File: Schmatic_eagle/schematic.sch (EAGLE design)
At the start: 7 parts, among them IC1 MEGA16-M, IC2 MC145026D, M1 WIRELESS-XY-FST

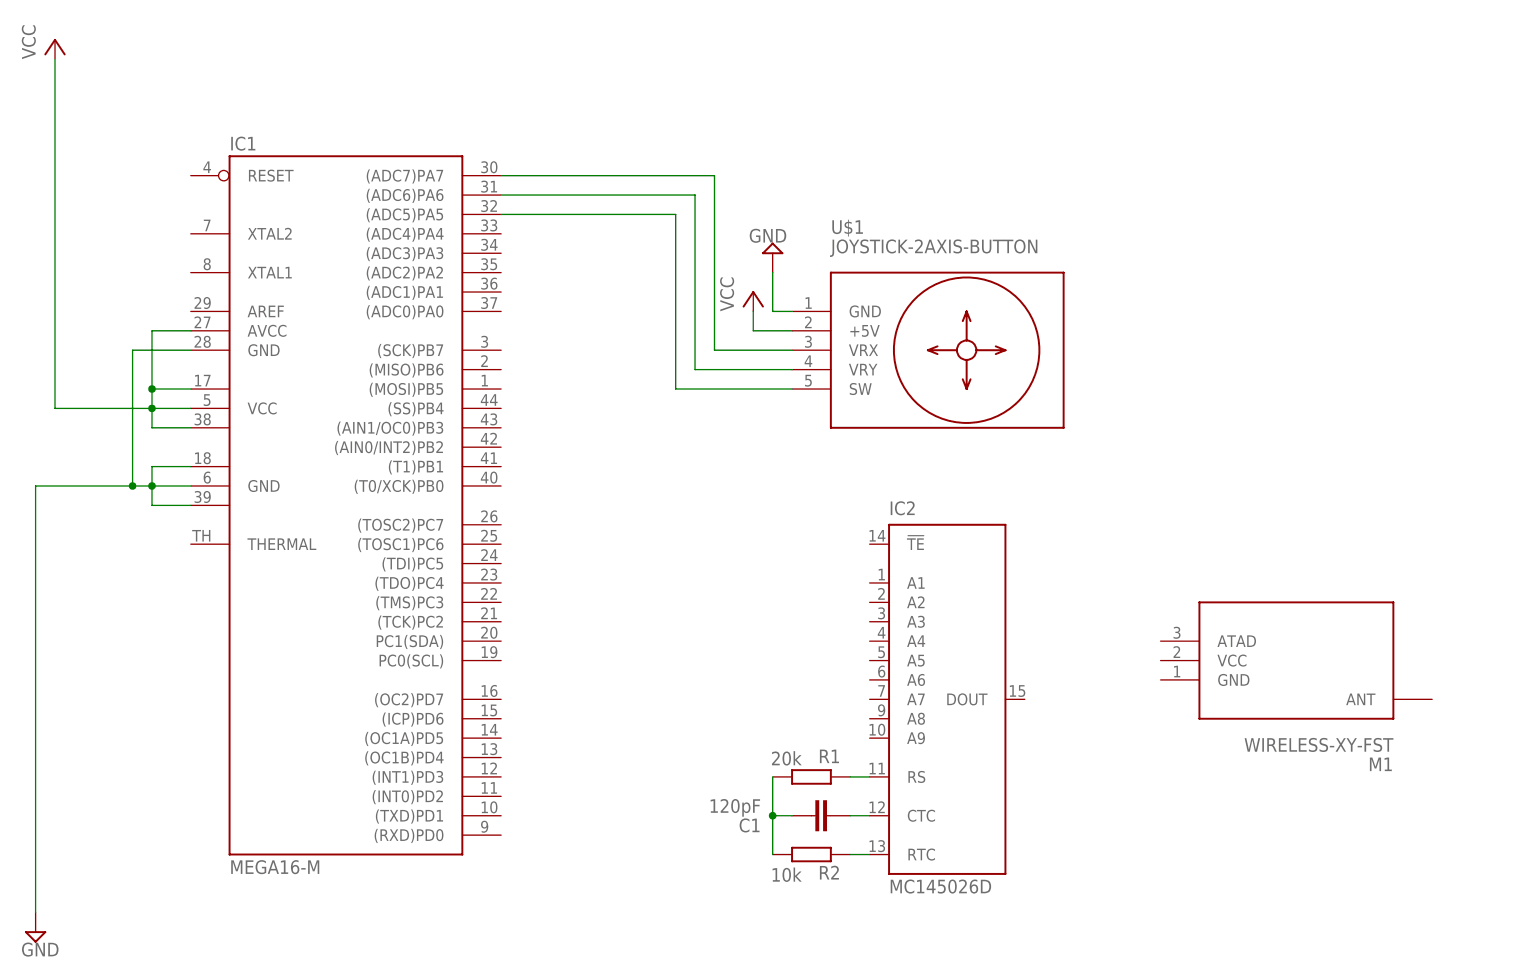
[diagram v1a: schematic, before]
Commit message: Schematic updates
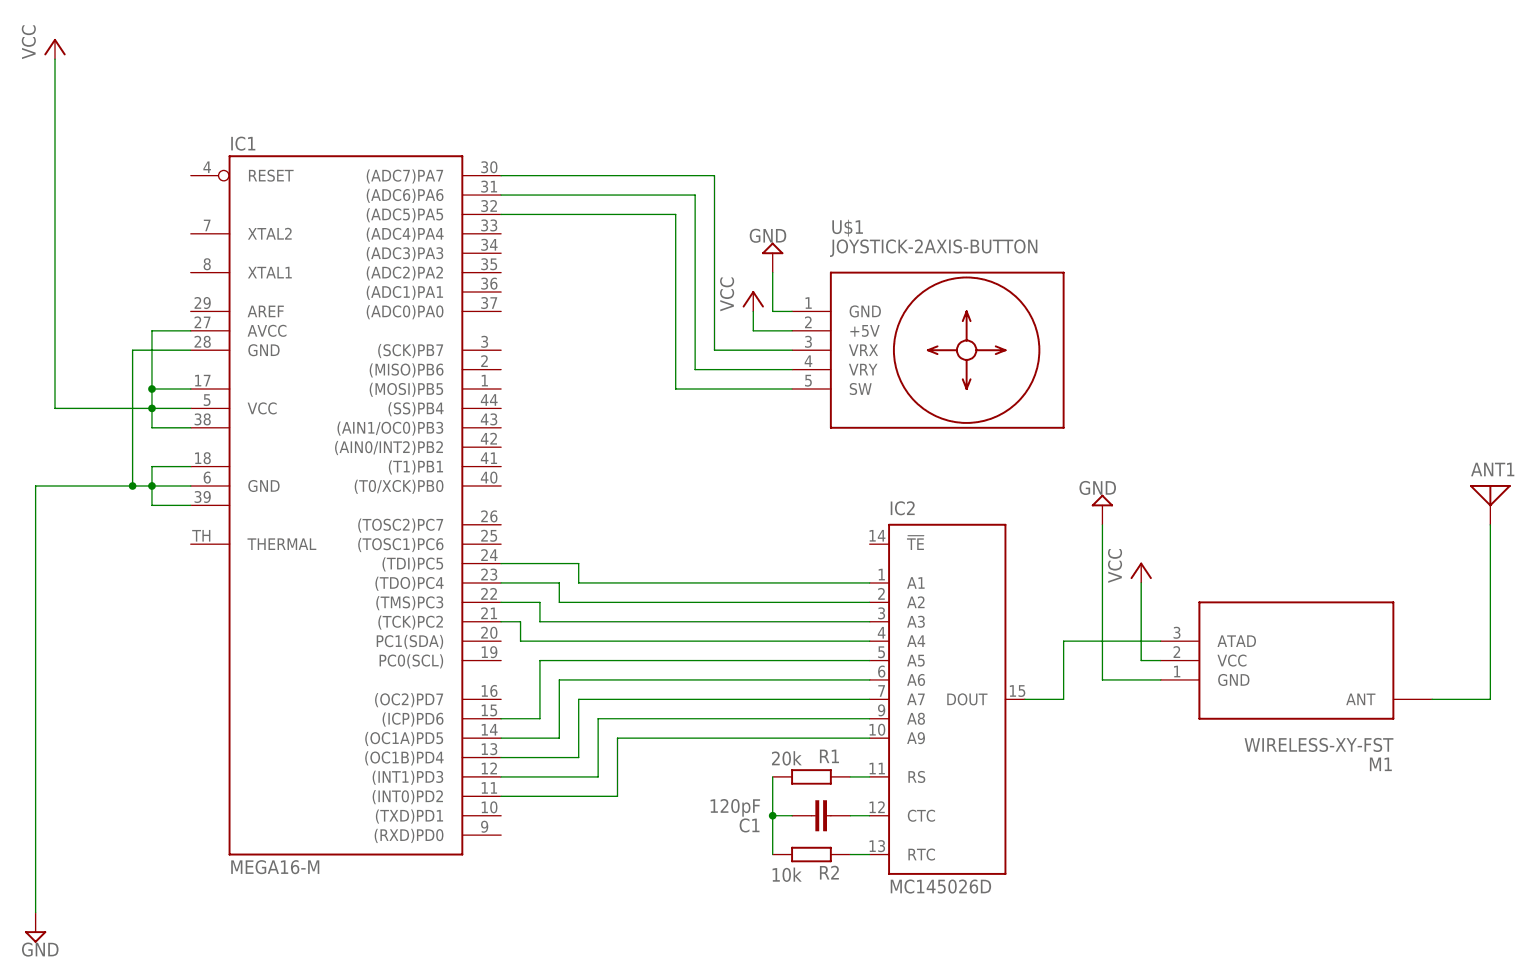
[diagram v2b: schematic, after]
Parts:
- added ANT1: (no value), discrete:ANTENNA
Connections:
- new net N$10: IC1.(OC1B)PD4, IC2G$1.A7
- new net N$11: IC1.(OC1A)PD5, IC2G$1.A6
- new net N$12: IC1.(ICP)PD6, IC2G$1.A5
- new net N$13: IC1.(INT0)PD2, IC2G$1.A9
- new net N$14: IC1.(INT1)PD3, IC2G$1.A8
- new net N$15: IC1.(TCK)PC2, IC2G$1.A4
- new net N$16: IC1.(TMS)PC3, IC2G$1.A3
- new net N$17: IC1.(TDO)PC4, IC2G$1.A2
- new net N$18: IC1.(TDI)PC5, IC2G$1.A1
- new net N$8: IC2G$1.DOUT, M1.ATAD
- new net N$9: ANT1.1, M1.ANT
- net GND: now also M1.GND
- net VCC: now also M1.VCC
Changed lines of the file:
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@@
 <part name="R1" library="rcl" library_urn="urn:adsk.eagle:library:334" deviceset="R-EU_" device="01005" package3d_urn="urn:adsk.eagle:package:26133/2" value="20k"/>
 <part name="R2" library="rcl" library_urn="urn:adsk.eagle:library:334" deviceset="R-EU_" device="01005" package3d_urn="urn:adsk.eagle:package:26133/2" value="10k"/>
+<part name="P+3" library="supply1" library_urn="urn:adsk.eagle:library:371" deviceset="VCC" device=""/>
+<part name="SUPPLY3" library="supply2" library_urn="urn:adsk.eagle:library:372" deviceset="GND" device=""/>
+<part name="ANT1" library="discrete" library_urn="urn:adsk.eagle:library:211" deviceset="ANTENNA" device="" package3d_urn="urn:adsk.eagle:package:12928/1"/>
 </parts>
 <sheets>
@@
 <attribute name="NAME" x="229.87" y="67.0814" size="1.778" layer="95" rot="R180"/>
 <attribute name="VALUE" x="224.79" y="66.802" size="1.778" layer="96" rot="R180"/>
+</instance>
+<instance part="P+3" gate="VCC" x="269.24" y="106.68" smashed="yes">
+<attribute name="VALUE" x="266.7" y="104.14" size="1.778" layer="96" rot="R90"/>
+</instance>
+<instance part="SUPPLY3" gate="GND" x="264.16" y="114.3" smashed="yes" rot="R180">
+<attribute name="VALUE" x="266.065" y="117.475" size="1.778" layer="96" rot="R180"/>
+</instance>
+<instance part="ANT1" gate="A" x="314.96" y="116.84" smashed="yes">
+<attribute name="NAME" x="312.42" y="118.11" size="1.778" layer="95"/>
+<attribute name="VALUE" x="317.5" y="111.76" size="1.778" layer="96"/>
 </instance>
 </instances>
@@
 <wire x1="139.7" y1="137.16" x2="139.7" y2="129.54" width="0.1524" layer="91"/>
 <junction x="139.7" y="129.54"/>
+</segment>
+<segment>
+<pinref part="P+3" gate="VCC" pin="VCC"/>
+<wire x1="269.24" y1="104.14" x2="269.24" y2="93.98" width="0.1524" layer="91"/>
+<pinref part="M1" gate="G$1" pin="VCC"/>
+<wire x1="269.24" y1="93.98" x2="271.78" y2="93.98" width="0.1524" layer="91"/>
 </segment>
 </net>
@@
 <junction x="137.16" y="116.84"/>
 </segment>
+<segment>
+<pinref part="SUPPLY3" gate="GND" pin="GND"/>
+<pinref part="M1" gate="G$1" pin="GND"/>
+<wire x1="264.16" y1="111.76" x2="264.16" y2="91.44" width="0.1524" layer="91"/>
+<wire x1="264.16" y1="91.44" x2="271.78" y2="91.44" width="0.1524" layer="91"/>
+</segment>
 </net>
 <net name="N$4" class="0">
@@
 </segment>
 </net>
+<net name="N$8" class="0">
+<segment>
+<pinref part="M1" gate="G$1" pin="ATAD"/>
+<wire x1="271.78" y1="96.52" x2="259.08" y2="96.52" width="0.1524" layer="91"/>
+<wire x1="259.08" y1="96.52" x2="259.08" y2="88.9" width="0.1524" layer="91"/>
+<pinref part="IC2" gate="G$1" pin="DOUT"/>
+<wire x1="259.08" y1="88.9" x2="254" y2="88.9" width="0.1524" layer="91"/>
+</segment>
+</net>
+<net name="N$9" class="0">
+<segment>
+<pinref part="ANT1" gate="A" pin="1"/>
+<pinref part="M1" gate="G$1" pin="ANT"/>
+<wire x1="314.96" y1="111.76" x2="314.96" y2="88.9" width="0.1524" layer="91"/>
+<wire x1="314.96" y1="88.9" x2="307.34" y2="88.9" width="0.1524" layer="91"/>
+</segment>
+</net>
+<net name="N$13" class="0">
+<segment>
+<pinref part="IC2" gate="G$1" pin="A9"/>
+<wire x1="233.68" y1="83.82" x2="200.66" y2="83.82" width="0.1524" layer="91"/>
+<wire x1="200.66" y1="83.82" x2="200.66" y2="76.2" width="0.1524" layer="91"/>
+<pinref part="IC1" gate="G$1" pin="(INT0)PD2"/>
+<wire x1="200.66" y1="76.2" x2="185.42" y2="76.2" width="0.1524" layer="91"/>
+</segment>
+</net>
+<net name="N$14" class="0">
+<segment>
+<pinref part="IC2" gate="G$1" pin="A8"/>
+<wire x1="233.68" y1="86.36" x2="198.12" y2="86.36" width="0.1524" layer="91"/>
+<wire x1="198.12" y1="86.36" x2="198.12" y2="78.74" width="0.1524" layer="91"/>
+<pinref part="IC1" gate="G$1" pin="(INT1)PD3"/>
+<wire x1="198.12" y1="78.74" x2="185.42" y2="78.74" width="0.1524" layer="91"/>
+</segment>
+</net>
+<net name="N$10" class="0">
+<segment>
+<pinref part="IC1" gate="G$1" pin="(OC1B)PD4"/>
+<wire x1="185.42" y1="81.28" x2="195.58" y2="81.28" width="0.1524" layer="91"/>
+<wire x1="195.58" y1="81.28" x2="195.58" y2="88.9" width="0.1524" layer="91"/>
+<pinref part="IC2" gate="G$1" pin="A7"/>
+<wire x1="233.68" y1="88.9" x2="195.58" y2="88.9" width="0.1524" layer="91"/>
+</segment>
+</net>
+<net name="N$11" class="0">
+<segment>
+<pinref part="IC2" gate="G$1" pin="A6"/>
+<wire x1="233.68" y1="91.44" x2="193.04" y2="91.44" width="0.1524" layer="91"/>
+<wire x1="193.04" y1="91.44" x2="193.04" y2="83.82" width="0.1524" layer="91"/>
+<pinref part="IC1" gate="G$1" pin="(OC1A)PD5"/>
+<wire x1="193.04" y1="83.82" x2="185.42" y2="83.82" width="0.1524" layer="91"/>
+</segment>
+</net>
+<net name="N$12" class="0">
+<segment>
+<pinref part="IC2" gate="G$1" pin="A5"/>
+<wire x1="233.68" y1="93.98" x2="190.5" y2="93.98" width="0.1524" layer="91"/>
+<wire x1="190.5" y1="93.98" x2="190.5" y2="86.36" width="0.1524" layer="91"/>
+<pinref part="IC1" gate="G$1" pin="(ICP)PD6"/>
+<wire x1="190.5" y1="86.36" x2="185.42" y2="86.36" width="0.1524" layer="91"/>
+</segment>
+</net>
+<net name="N$15" class="0">
+<segment>
+<pinref part="IC2" gate="G$1" pin="A4"/>
+<wire x1="233.68" y1="96.52" x2="187.96" y2="96.52" width="0.1524" layer="91"/>
+<wire x1="187.96" y1="96.52" x2="187.96" y2="99.06" width="0.1524" layer="91"/>
+<pinref part="IC1" gate="G$1" pin="(TCK)PC2"/>
+<wire x1="187.96" y1="99.06" x2="185.42" y2="99.06" width="0.1524" layer="91"/>
+</segment>
+</net>
+<net name="N$16" class="0">
+<segment>
+<pinref part="IC1" gate="G$1" pin="(TMS)PC3"/>
+<wire x1="185.42" y1="101.6" x2="190.5" y2="101.6" width="0.1524" layer="91"/>
+<wire x1="190.5" y1="101.6" x2="190.5" y2="99.06" width="0.1524" layer="91"/>
+<pinref part="IC2" gate="G$1" pin="A3"/>
+<wire x1="190.5" y1="99.06" x2="233.68" y2="99.06" width="0.1524" layer="91"/>
+</segment>
+</net>
+<net name="N$17" class="0">
+<segment>
+<pinref part="IC1" gate="G$1" pin="(TDO)PC4"/>
+<wire x1="185.42" y1="104.14" x2="193.04" y2="104.14" width="0.1524" layer="91"/>
+<wire x1="193.04" y1="104.14" x2="193.04" y2="101.6" width="0.1524" layer="91"/>
+<pinref part="IC2" gate="G$1" pin="A2"/>
+<wire x1="193.04" y1="101.6" x2="233.68" y2="101.6" width="0.1524" layer="91"/>
+</segment>
+</net>
+<net name="N$18" class="0">
+<segment>
+<pinref part="IC1" gate="G$1" pin="(TDI)PC5"/>
+<wire x1="185.42" y1="106.68" x2="195.58" y2="106.68" width="0.1524" layer="91"/>
+<pinref part="IC2" gate="G$1" pin="A1"/>
+<wire x1="195.58" y1="106.68" x2="195.58" y2="104.14" width="0.1524" layer="91"/>
+<wire x1="195.58" y1="104.14" x2="233.68" y2="104.14" width="0.1524" layer="91"/>
+</segment>
+</net>

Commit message: Schematic updates
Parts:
- added C2: 0.1uF, capacitor-wima:C2,5-3
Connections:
- new net N$19: IC1.(TOSC1)PC6, IC2G$1.!TE
- net GND: now also C2.1
- net VCC: now also C2.2
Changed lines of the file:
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@@
 <part name="SUPPLY3" library="supply2" library_urn="urn:adsk.eagle:library:372" deviceset="GND" device=""/>
 <part name="ANT1" library="discrete" library_urn="urn:adsk.eagle:library:211" deviceset="ANTENNA" device="" package3d_urn="urn:adsk.eagle:package:12928/1"/>
+<part name="SUPPLY4" library="supply2" library_urn="urn:adsk.eagle:library:372" deviceset="GND" device=""/>
+<part name="P+4" library="supply1" library_urn="urn:adsk.eagle:library:371" deviceset="VCC" device=""/>
+<part name="C2" library="capacitor-wima" library_urn="urn:adsk.eagle:library:116" deviceset="C" device="2,5-3" package3d_urn="urn:adsk.eagle:package:5436/1" value="0.1uF"/>
 </parts>
 <sheets>
@@
 <attribute name="NAME" x="312.42" y="118.11" size="1.778" layer="95"/>
 <attribute name="VALUE" x="317.5" y="111.76" size="1.778" layer="96"/>
+</instance>
+<instance part="SUPPLY4" gate="GND" x="289.56" y="114.3" smashed="yes">
+<attribute name="VALUE" x="287.655" y="111.125" size="1.778" layer="96"/>
+</instance>
+<instance part="P+4" gate="VCC" x="289.56" y="132.08" smashed="yes">
+<attribute name="VALUE" x="287.02" y="129.54" size="1.778" layer="96" rot="R90"/>
+</instance>
+<instance part="C2" gate="G$1" x="289.56" y="121.92" smashed="yes" rot="R180">
+<attribute name="NAME" x="292.481" y="122.936" size="1.778" layer="95" rot="R270"/>
+<attribute name="VALUE" x="295.021" y="125.476" size="1.778" layer="96" rot="R270"/>
 </instance>
 </instances>
@@
 <pinref part="M1" gate="G$1" pin="VCC"/>
 <wire x1="269.24" y1="93.98" x2="271.78" y2="93.98" width="0.1524" layer="91"/>
+</segment>
+<segment>
+<pinref part="C2" gate="G$1" pin="2"/>
+<pinref part="P+4" gate="VCC" pin="VCC"/>
+<wire x1="289.56" y1="127" x2="289.56" y2="129.54" width="0.1524" layer="91"/>
 </segment>
 </net>
@@
 <wire x1="264.16" y1="91.44" x2="271.78" y2="91.44" width="0.1524" layer="91"/>
 </segment>
+<segment>
+<pinref part="SUPPLY4" gate="GND" pin="GND"/>
+<pinref part="C2" gate="G$1" pin="1"/>
+<wire x1="289.56" y1="116.84" x2="289.56" y2="119.38" width="0.1524" layer="91"/>
+</segment>
 </net>
 <net name="N$4" class="0">
@@
 </segment>
 </net>
+<net name="N$19" class="0">
+<segment>
+<pinref part="IC1" gate="G$1" pin="(TOSC1)PC6"/>
+<pinref part="IC2" gate="G$1" pin="!TE"/>
+<wire x1="185.42" y1="109.22" x2="233.68" y2="109.22" width="0.1524" layer="91"/>
+</segment>
+</net>

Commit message: Schematic updates
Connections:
- net VCC: now also IC1.AREF
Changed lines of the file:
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@@
 <wire x1="139.7" y1="137.16" x2="139.7" y2="129.54" width="0.1524" layer="91"/>
 <junction x="139.7" y="129.54"/>
+<pinref part="IC1" gate="G$1" pin="AREF"/>
+<wire x1="144.78" y1="139.7" x2="139.7" y2="139.7" width="0.1524" layer="91"/>
+<wire x1="139.7" y1="139.7" x2="139.7" y2="137.16" width="0.1524" layer="91"/>
+<junction x="139.7" y="137.16"/>
 </segment>
 <segment>
